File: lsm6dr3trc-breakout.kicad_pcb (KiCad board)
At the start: 2 copper layers, 13.2 x 18.3 mm, 13 parts, among them CN1 AFC10-S04QCA-00, CN2 AFC10-S04QCA-00, J1 Conn_01x06_Pin, J2 Conn_01x04_Pin, U1 LSM6DS3TR-C

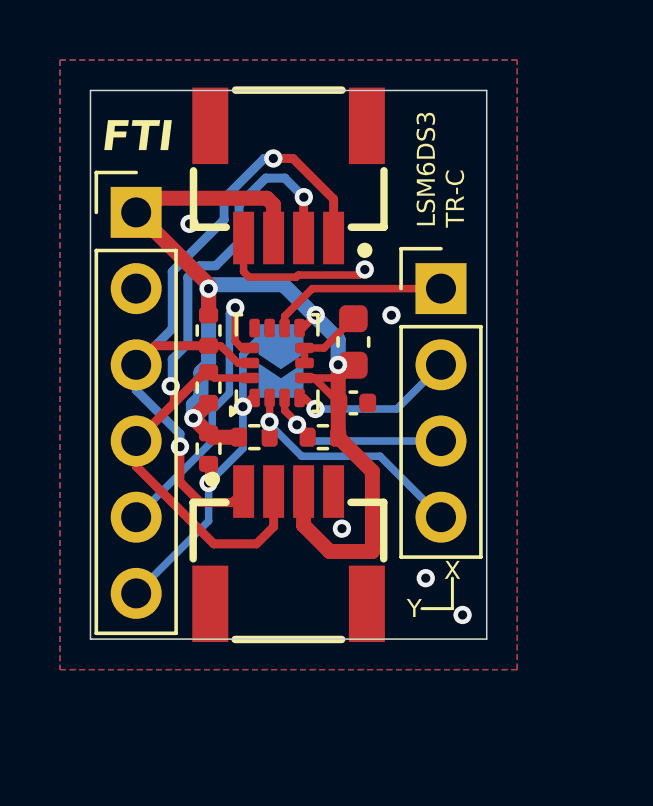
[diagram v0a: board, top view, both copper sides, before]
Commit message: fix qwiic pinout, redo footprint
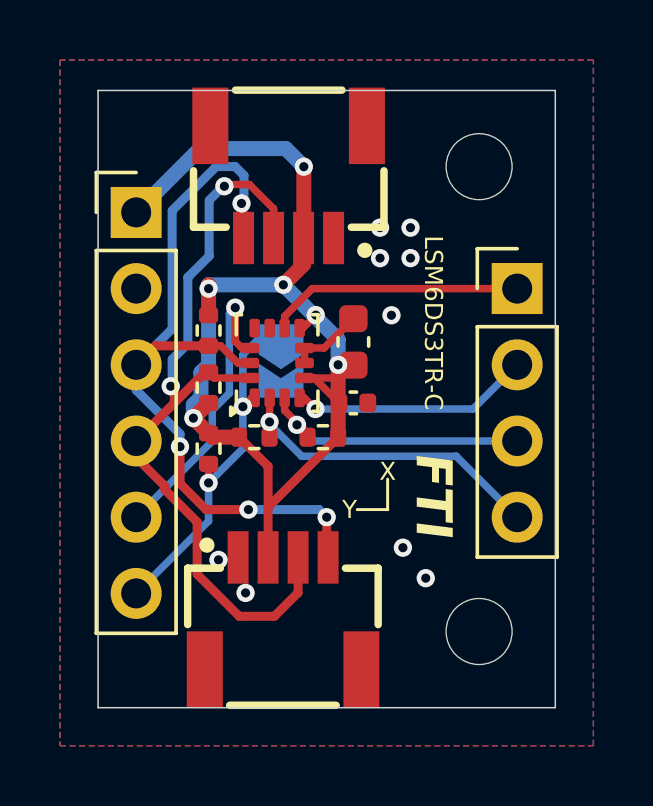
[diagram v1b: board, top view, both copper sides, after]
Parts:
- added H1: MountingHole, MountingHole:MountingHole_2.2mm_M2, F.Cu at (113.0, 85.1)
- added H2: MountingHole, MountingHole:MountingHole_2.2mm_M2, F.Cu at (113.0, 69.6)
- moved J2 2.54 mm to (114.3, 73.7)
- moved CN2 2.20 mm to (106.5, 84.5)
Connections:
- CN1 pad 1: /SCL -> GND
- CN1 pad 2: /SDA -> VDD
- CN1 pad 3: VDD -> /SDA
- CN1 pad 4: GND -> /SCL
- CN1 pad 5: unconnected-(CN1-Pad5) -> GND
- CN1 pad 6: unconnected-(CN1-Pad6) -> GND
- CN2 pad 1: /SCL -> GND
- CN2 pad 2: /SDA -> VDD
- CN2 pad 3: VDD -> /SDA
- CN2 pad 4: GND -> /SCL
- CN2 pad 5: unconnected-(CN2-Pad5) -> GND
- CN2 pad 6: unconnected-(CN2-Pad6) -> GND
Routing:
- net GND: track 7.88 -> 2.53 mm, vias 6 -> 9
- net /XDA: track 8.26 -> 10.8 mm
- net /INT1: track 5.48 -> 8.02 mm
- net /XCL: track 6.58 -> 9.12 mm
- net /INT2: track 5.99 -> 8.53 mm
- net /SCL: track 24.2 -> 26.5 mm, vias 2 -> 4
- net /SDA: track 24.8 -> 26.5 mm
- net VDD: track 38.4 -> 39.6 mm, vias 4 -> 6
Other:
- board size 13.2 x 18.3 mm -> 15.2 x 20.6 mm
- board text added: "3V3"
- board text added: "LSM6DS3TR-C"
- board text removed: "LSM6DS3 TR-C"
- board text removed: "VDD"
